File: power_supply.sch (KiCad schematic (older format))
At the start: 44 parts

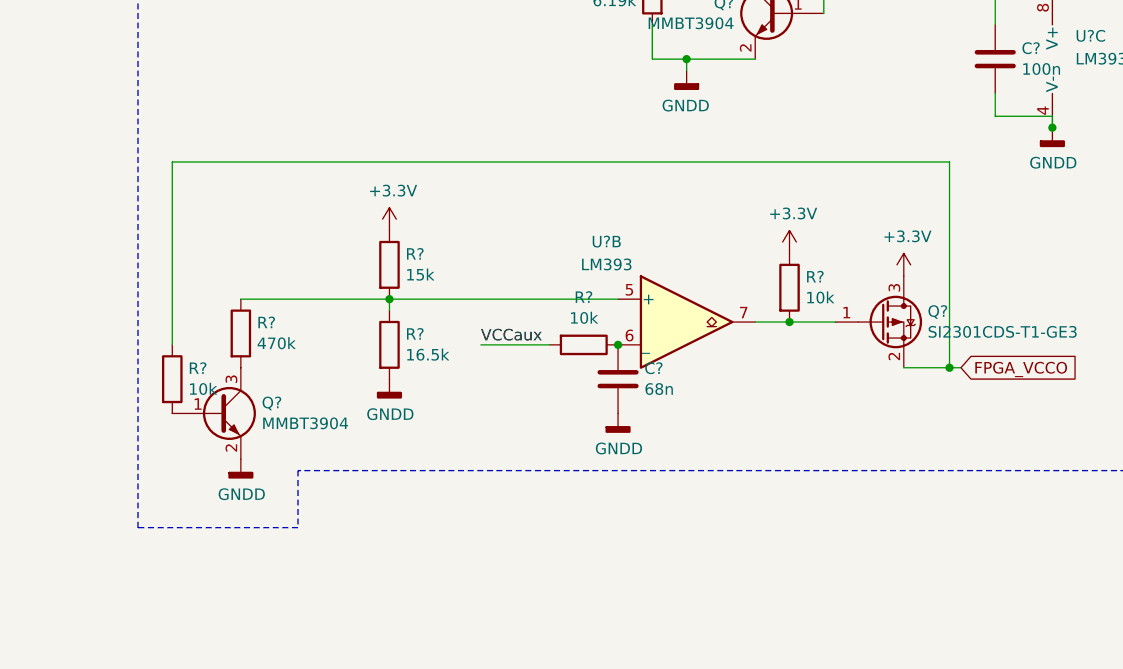
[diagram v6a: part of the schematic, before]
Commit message: one less transistor is enough
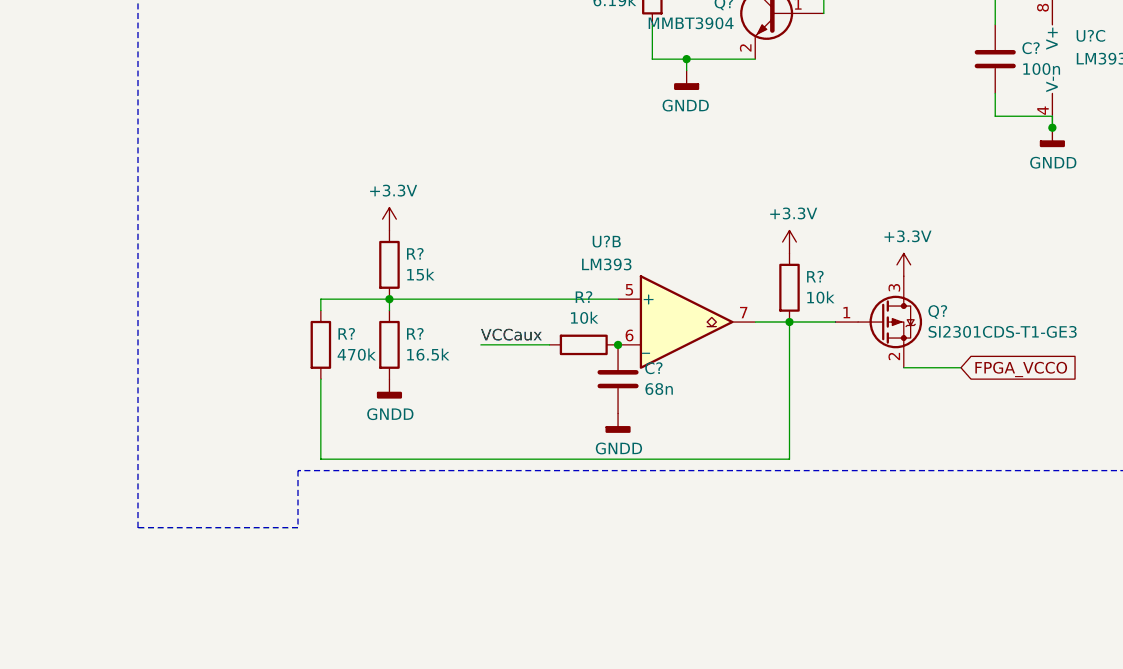
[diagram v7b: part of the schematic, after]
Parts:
- removed Q?: MMBT3904, symbol Device:Q_NPN_BEC
- removed R?: 10k, symbol Device:R
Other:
- moved on the sheet: R?
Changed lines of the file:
@@
 Text GLabel 7500 5950 2    50   Input ~ 0
 FPGA_VCCO
-Wire Wire Line
-	7500 5950 7450 5950
 $Comp
 L Device:R R?
@@
 L Device:R R?
 U 1 1 60508322
-P 4350 5800
-F 0 "R?" H 4420 5846 50  0000 L CNN
-F 1 "470k" H 4420 5755 50  0000 L CNN
-F 2 "" V 4280 5800 50  0001 C CNN
-F 3 "~" H 4350 5800 50  0001 C CNN
-	1    4350 5800
-	1    0    0    -1
-$EndComp
-Wire Wire Line
-	4350 5650 5000 5650
-$Comp
-L power:GNDD #PWR?
-U 1 1 6050CC3B
-P 4350 6350
-F 0 "#PWR?" H 4350 6100 50  0001 C CNN
-F 1 "GNDD" H 4354 6195 50  0000 C CNN
-F 2 "" H 4350 6350 50  0001 C CNN
-F 3 "" H 4350 6350 50  0001 C CNN
-	1    4350 6350
-	1    0    0    -1
-$EndComp
-$Comp
-L Device:R R?
-U 1 1 6050D4AF
-P 4050 6000
-F 0 "R?" H 4120 6046 50  0000 L CNN
-F 1 "10k" H 4120 5955 50  0000 L CNN
-F 2 "" V 3980 6000 50  0001 C CNN
-F 3 "~" H 4050 6000 50  0001 C CNN
-	1    4050 6000
-	1    0    0    -1
-$EndComp
-Wire Wire Line
-	4050 5850 4050 5050
-Wire Wire Line
-	4050 5050 7450 5050
-Wire Wire Line
-	7450 5050 7450 5950
-Connection ~ 7450 5950
-Wire Wire Line
-	7450 5950 7250 5950
+P 4700 5850
+F 0 "R?" H 4770 5896 50  0000 L CNN
+F 1 "470k" H 4770 5805 50  0000 L CNN
+F 2 "" V 4630 5850 50  0001 C CNN
+F 3 "~" H 4700 5850 50  0001 C CNN
+	1    4700 5850
+	1    0    0    -1
+$EndComp
 $Comp
 L power:GNDD #PWR?
@@
 $EndComp
 $Comp
-L Device:Q_NPN_BEC Q?
-U 1 1 60524F5B
-P 4250 6150
-F 0 "Q?" H 4441 6196 50  0000 L CNN
-F 1 "MMBT3904" H 4441 6105 50  0000 L CNN
-F 2 "" H 4450 6250 50  0001 C CNN
-F 3 "~" H 4250 6150 50  0001 C CNN
-	1    4250 6150
-	1    0    0    -1
-$EndComp
-$Comp
 L Device:Q_PMOS_GSD Q?
 U 1 1 60525B4A
@@
 Text Notes 4000 4350 0    50   ~ 0
 Power on sequencing with comparators. \nFirst VCCint and VCCbram start, \nthen we switch on VCCaux and then VCCo\n
+Wire Wire Line
+	7250 5950 7500 5950
+Wire Wire Line
+	4700 6000 4700 6350
+Wire Wire Line
+	4700 6350 6750 6350
+Wire Wire Line
+	6750 6350 6750 5750
+Wire Wire Line
+	4700 5700 4700 5650
+Wire Wire Line
+	4700 5650 5000 5650
 $EndSCHEMATC
